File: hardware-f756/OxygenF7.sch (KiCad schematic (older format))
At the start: 39 parts, among them J1 Conn_01x04, J2 USB_C_2.0, SW1 SW_Push, SW2 SW_Push, U1 STM32F756VGTx, U2 AP2112K-3.3, Y1 8Mhz

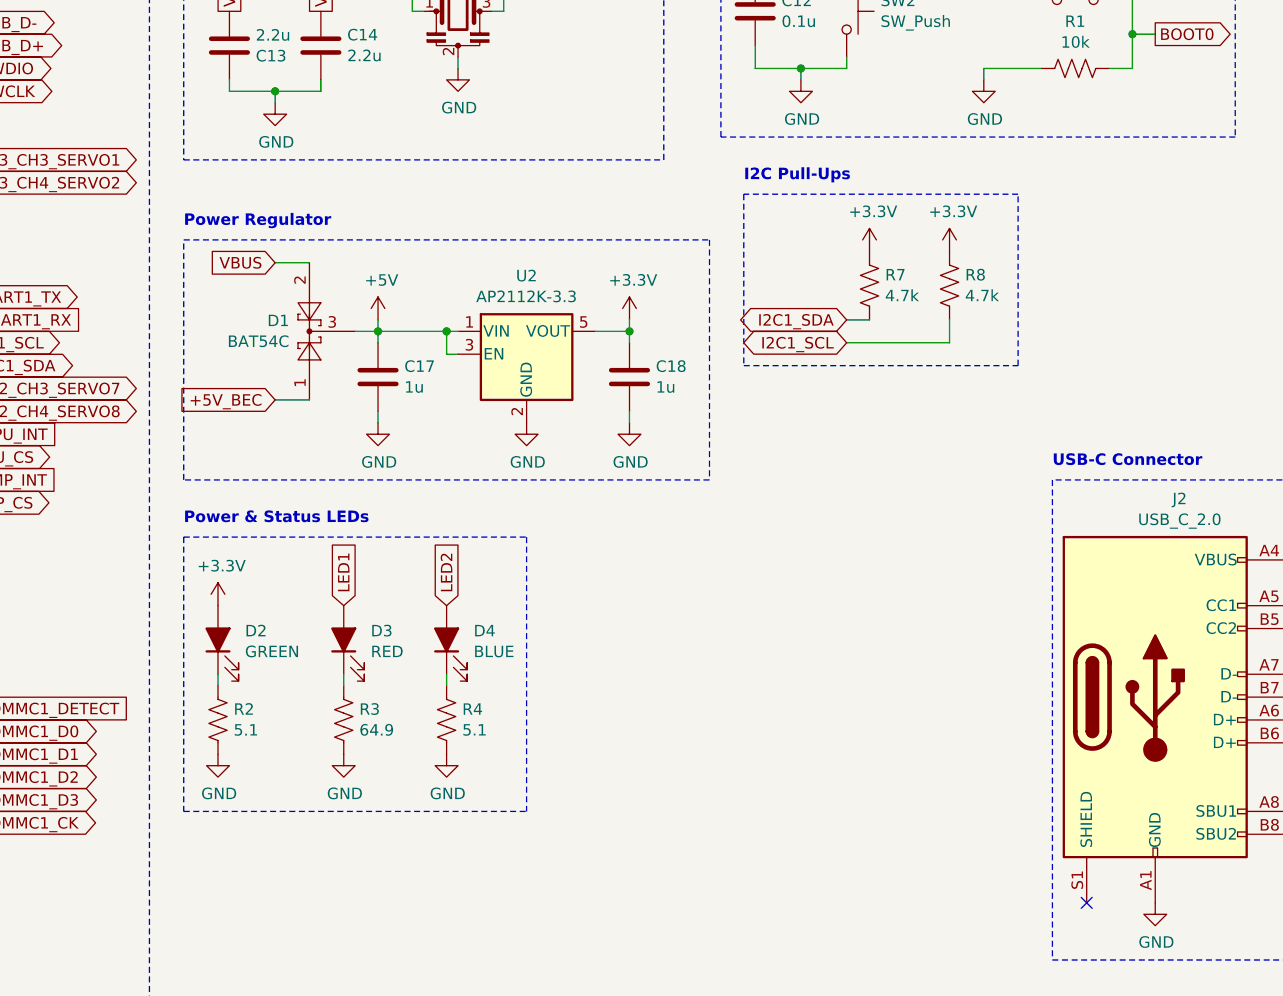
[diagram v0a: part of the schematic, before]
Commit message: Swap out some out-of-stock parts
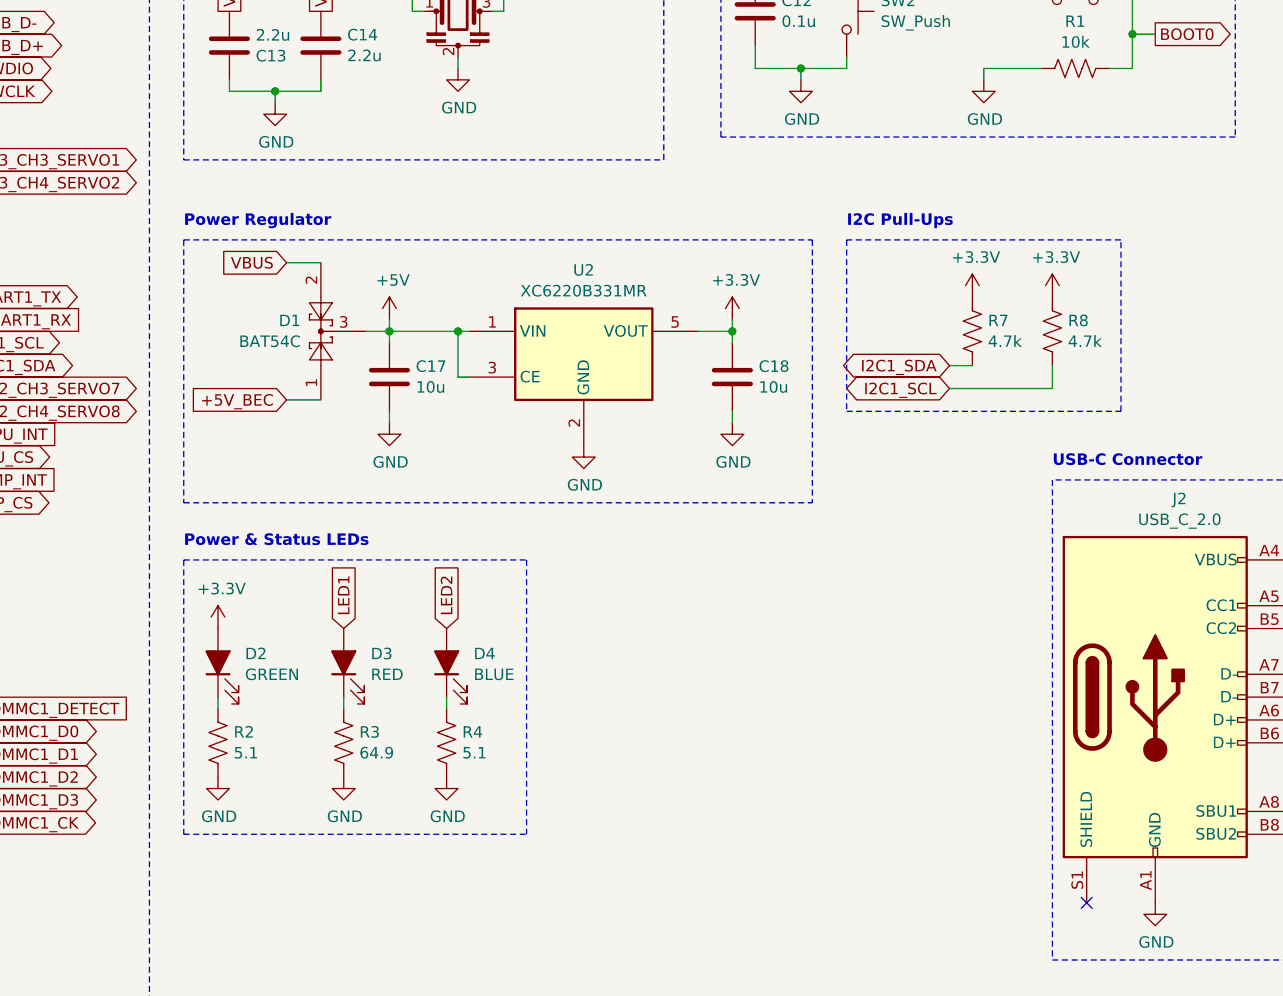
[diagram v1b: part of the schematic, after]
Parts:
- removed U2: AP2112K-3.3, Package_TO_SOT_SMD:SOT-23-5, symbol Regulator_Linear:AP2112K-3.3
- added U2: XC6220B331MR, Package_TO_SOT_SMD:SOT-23-5, symbol Regulator_Linear:XC6220B331MR
- C10, C11, C12, C2, C3, C4, C5, C6, C8: Part# CL21B104KACNNNC -> CL21B104KBCNNNC‎
- C17, C18: value 1u -> 10u; Part# CL21B105KOFNNNG -> CL21B106KQQNNNG
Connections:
- net +3V3: now also U2.5 (VOUT)
- net +5V: now also U2.1 (VIN), U2.3 (CE)
- net GND: now also U2.2 (GND)
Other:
- moved on the sheet: C17, C18, D1, D2, D3, D4, R2, R3, R4, R7, R8

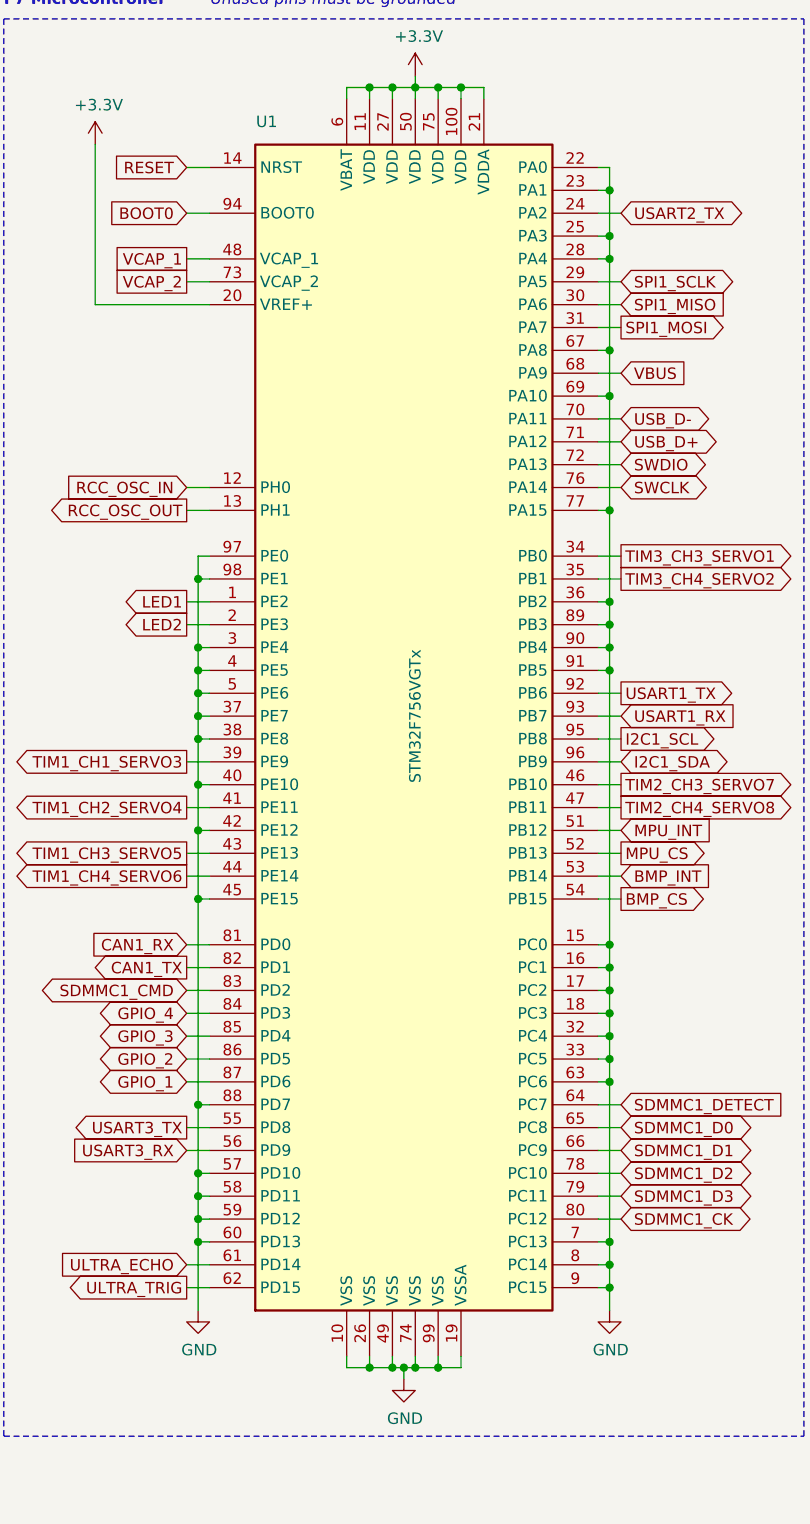
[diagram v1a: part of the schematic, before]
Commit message: Don't ground unused MCU pins and add microSD pull-up resistors
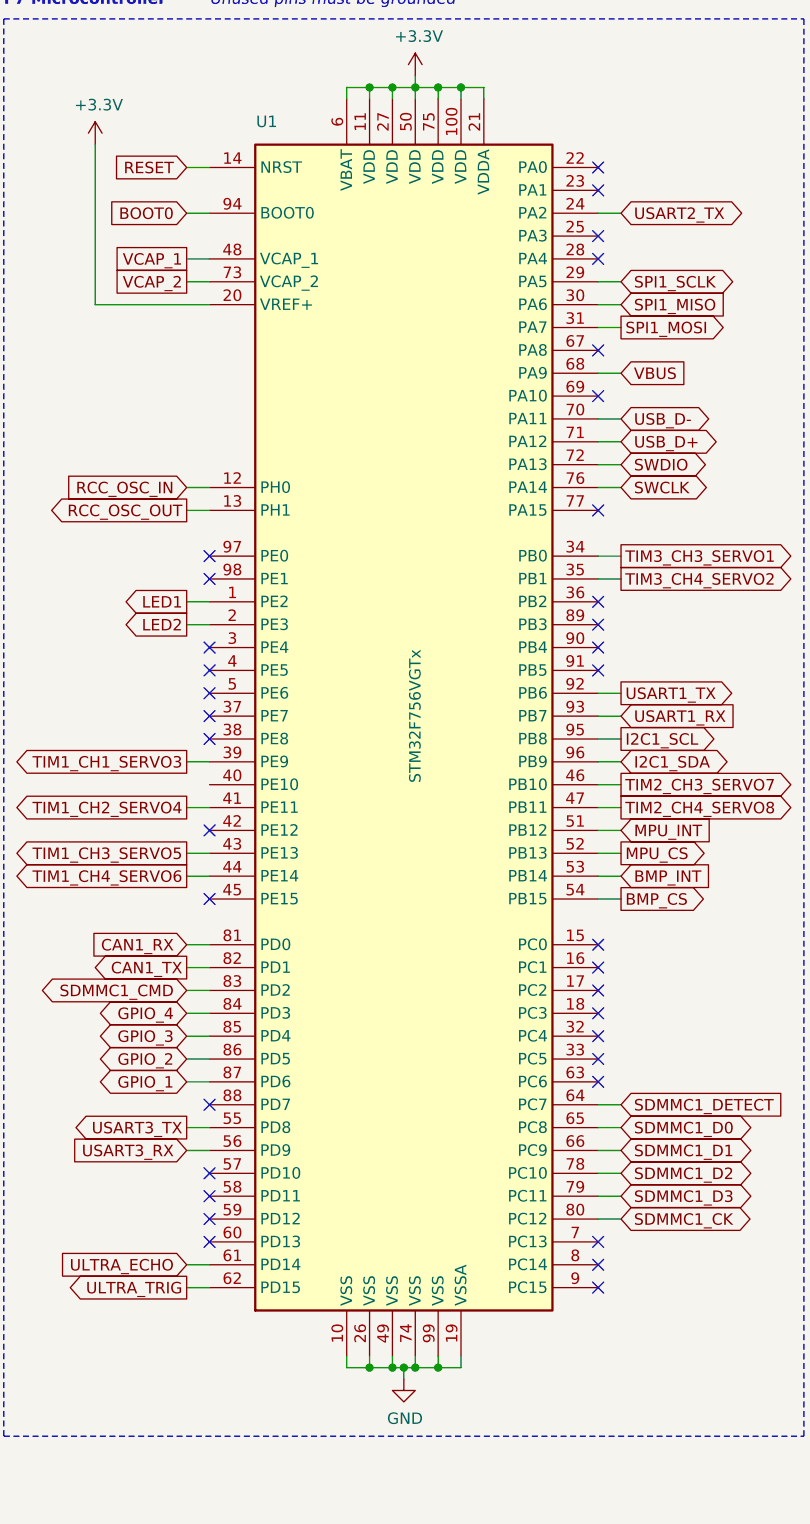
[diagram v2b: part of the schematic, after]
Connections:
- net GND: no longer U1.15 (PC0), U1.16 (PC1), U1.17 (PC2), U1.18 (PC3), U1.22 (PA0), U1.23 (PA1), U1.25 (PA3), U1.28 (PA4), U1.3 (PE4), U1.32 (PC4), U1.33 (PC5), U1.36 (PB2), U1.37 (PE7), U1.38 (PE8), U1.4 (PE5), U1.40 (PE10), U1.42 (PE12), U1.45 (PE15), U1.5 (PE6), U1.57 (PD10), U1.58 (PD11), U1.59 (PD12), U1.60 (PD13), U1.63 (PC6), U1.67 (PA8), U1.69 (PA10), U1.7 (PC13), U1.77 (PA15), U1.8 (PC14), U1.88 (PD7), U1.89 (PB3), U1.9 (PC15), U1.90 (PB4), U1.91 (PB5), U1.97 (PE0), U1.98 (PE1)
- no-connect marks 3 -> 38
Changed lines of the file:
@@
 Wire Wire Line
 	3200 4550 3300 4550
-$Comp
-L power:GND #PWR0101
-U 1 1 60858319
-P 1450 6350
-F 0 "#PWR0101" H 1450 6100 50  0001 C CNN
-F 1 "GND" H 1455 6177 50  0000 C CNN
-F 2 "" H 1450 6350 50  0001 C CNN
-F 3 "" H 1450 6350 50  0001 C CNN
-	1    1450 6350
-	1    0    0    -1
-$EndComp
-Wire Wire Line
-	1450 6350 1450 6050
-Wire Wire Line
-	1450 3050 1500 3050
-Wire Wire Line
-	1500 3150 1450 3150
-Connection ~ 1450 3150
-Wire Wire Line
-	1450 3150 1450 3050
-Wire Wire Line
-	1500 3450 1450 3450
-Connection ~ 1450 3450
-Wire Wire Line
-	1450 3450 1450 3150
-Wire Wire Line
-	1500 3550 1450 3550
-Connection ~ 1450 3550
-Wire Wire Line
-	1450 3550 1450 3450
-Wire Wire Line
-	1500 3650 1450 3650
-Connection ~ 1450 3650
-Wire Wire Line
-	1450 3650 1450 3550
-Wire Wire Line
-	1500 3750 1450 3750
-Connection ~ 1450 3750
-Wire Wire Line
-	1450 3750 1450 3650
-Wire Wire Line
-	1500 3850 1450 3850
-Connection ~ 1450 3850
-Wire Wire Line
-	1450 3850 1450 3750
-Wire Wire Line
-	1500 4050 1450 4050
-Connection ~ 1450 4050
-Wire Wire Line
-	1450 4050 1450 3850
-Wire Wire Line
-	1500 4250 1450 4250
-Connection ~ 1450 4250
-Wire Wire Line
-	1450 4250 1450 4050
-Wire Wire Line
-	1500 6050 1450 6050
-Connection ~ 1450 6050
-Wire Wire Line
-	1450 6050 1450 5950
-Wire Wire Line
-	1500 5950 1450 5950
-Connection ~ 1450 5950
-Wire Wire Line
-	1450 5950 1450 5850
-Wire Wire Line
-	1500 5850 1450 5850
-Connection ~ 1450 5850
-Wire Wire Line
-	1450 5850 1450 5750
-Wire Wire Line
-	1500 5750 1450 5750
-Connection ~ 1450 5750
-Wire Wire Line
-	1450 5750 1450 5450
-Wire Wire Line
-	1500 5450 1450 5450
-Connection ~ 1450 5450
-Wire Wire Line
-	1450 5450 1450 4550
-Wire Wire Line
-	1500 4550 1450 4550
-Connection ~ 1450 4550
-Wire Wire Line
-	1450 4550 1450 4250
-$Comp
-L power:GND #PWR0102
-U 1 1 609359FA
-P 3250 6350
-F 0 "#PWR0102" H 3250 6100 50  0001 C CNN
-F 1 "GND" H 3255 6177 50  0000 C CNN
-F 2 "" H 3250 6350 50  0001 C CNN
-F 3 "" H 3250 6350 50  0001 C CNN
-	1    3250 6350
-	1    0    0    -1
-$EndComp
-Wire Wire Line
-	3250 1350 3200 1350
-Wire Wire Line
-	3200 1450 3250 1450
-Connection ~ 3250 1450
-Wire Wire Line
-	3250 1450 3250 1350
-Wire Wire Line
-	3200 1650 3250 1650
-Connection ~ 3250 1650
-Wire Wire Line
-	3250 1650 3250 1450
-Wire Wire Line
-	3200 1750 3250 1750
-Connection ~ 3250 1750
-Wire Wire Line
-	3250 1750 3250 1650
-Wire Wire Line
-	3200 2150 3250 2150
-Connection ~ 3250 2150
-Wire Wire Line
-	3250 2150 3250 1750
-Wire Wire Line
-	3200 2350 3250 2350
-Connection ~ 3250 2350
-Wire Wire Line
-	3250 2350 3250 2150
-Wire Wire Line
-	3200 2850 3250 2850
-Connection ~ 3250 2850
-Wire Wire Line
-	3250 2850 3250 2350
-Wire Wire Line
-	3200 3250 3250 3250
-Connection ~ 3250 3250
-Wire Wire Line
-	3250 3250 3250 2850
-Wire Wire Line
-	3200 3350 3250 3350
-Connection ~ 3250 3350
-Wire Wire Line
-	3250 3350 3250 3250
-Wire Wire Line
-	3200 3450 3250 3450
-Connection ~ 3250 3450
-Wire Wire Line
-	3250 3450 3250 3350
 Wire Wire Line
 	3200 3850 3300 3850
-Wire Wire Line
-	3250 6350 3250 6250
-Wire Wire Line
-	3200 3550 3250 3550
-Connection ~ 3250 3550
-Wire Wire Line
-	3250 3550 3250 3450
-Wire Wire Line
-	3200 4750 3250 4750
-Connection ~ 3250 4750
-Wire Wire Line
-	3250 4750 3250 3550
-Wire Wire Line
-	3250 4850 3200 4850
-Connection ~ 3250 4850
-Wire Wire Line
-	3250 4850 3250 4750
-Wire Wire Line
-	3200 4950 3250 4950
-Connection ~ 3250 4950
-Wire Wire Line
-	3250 4950 3250 4850
-Wire Wire Line
-	3250 5050 3200 5050
-Connection ~ 3250 5050
-Wire Wire Line
-	3250 5050 3250 4950
-Wire Wire Line
-	3250 5150 3200 5150
-Connection ~ 3250 5150
-Wire Wire Line
-	3250 5150 3250 5050
-Wire Wire Line
-	3250 5250 3200 5250
-Connection ~ 3250 5250
-Wire Wire Line
-	3250 5250 3250 5150
-Wire Wire Line
-	3250 5350 3200 5350
-Connection ~ 3250 5350
-Wire Wire Line
-	3250 5350 3250 5250
-Wire Wire Line
-	3200 6050 3250 6050
-Connection ~ 3250 6050
-Wire Wire Line
-	3250 6050 3250 5350
-Wire Wire Line
-	3250 6050 3250 6150
-Wire Wire Line
-	3250 6150 3200 6150
-Connection ~ 3250 6150
-Wire Wire Line
-	3200 6250 3250 6250
-Connection ~ 3250 6250
-Wire Wire Line
-	3250 6250 3250 6150
 $Comp
 L Regulator_Linear:XC6220B331MR U2
@@
 Wire Notes Line
 	7000 3400 7000 4550
+NoConn ~ 3200 1350
+NoConn ~ 3200 1450
+NoConn ~ 3200 1650
+NoConn ~ 3200 1750
+NoConn ~ 3200 6250
+NoConn ~ 3200 6150
+NoConn ~ 3200 6050
+NoConn ~ 3200 5350
+NoConn ~ 3200 5250
+NoConn ~ 3200 5150
+NoConn ~ 3200 5050
+NoConn ~ 3200 4950
+NoConn ~ 3200 4850
+NoConn ~ 3200 4750
+NoConn ~ 1500 6050
+NoConn ~ 1500 5950
+NoConn ~ 1500 5850
+NoConn ~ 1500 5750
+NoConn ~ 1500 5450
+NoConn ~ 1500 4550
+NoConn ~ 1500 4250
+NoConn ~ 1500 3850
+NoConn ~ 1500 3750
+NoConn ~ 1500 3650
+NoConn ~ 1500 3550
+NoConn ~ 1500 3450
+NoConn ~ 1500 3150
+NoConn ~ 1500 3050
+NoConn ~ 3200 2150
+NoConn ~ 3200 2350
+NoConn ~ 3200 2850
+NoConn ~ 3200 3250
+NoConn ~ 3200 3350
+NoConn ~ 3200 3450
+NoConn ~ 3200 3550
 $EndSCHEMATC
